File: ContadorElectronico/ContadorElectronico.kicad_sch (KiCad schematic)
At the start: 25 parts, among them J1 Screw_Terminal_01x02, J2 Screw_Terminal_01x02, SW1 MODE, SW2 INC, SW3 DEC, U2 L7805, U4 LM358, U5 4N35, U6 4N35

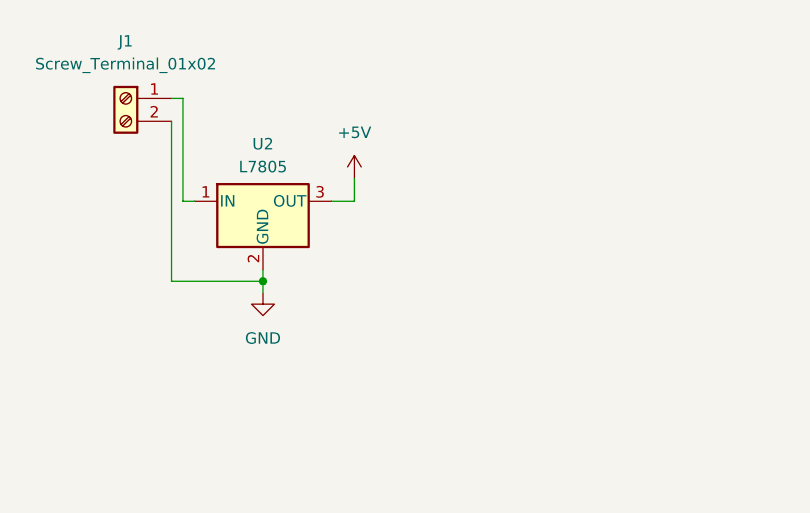
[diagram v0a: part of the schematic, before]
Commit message: Creación simbolo regulador 2596
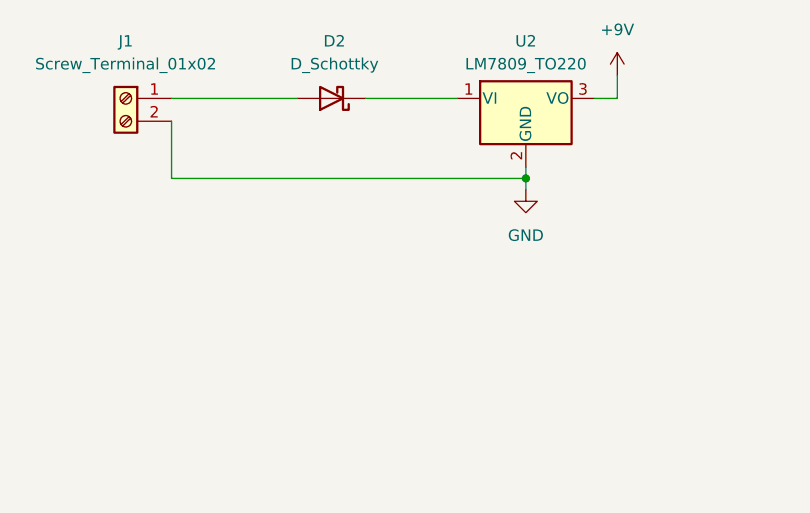
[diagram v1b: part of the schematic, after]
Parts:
- removed U2: L7805, Package_TO_SOT_THT:TO-220-3_Vertical, symbol Regulator_Linear:L7805
- added D2: D_Schottky, Diode_THT:D_DO-15_P12.70mm_Horizontal, symbol Device:D_Schottky
- added U2: LM7809_TO220, Package_TO_SOT_THT:TO-220-3_Vertical, symbol Regulator_Linear:LM7809_TO220
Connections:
- net GND: now also U2.2 (GND)
- net at J1.1 (Pin_1): now also D2.2 (A)
- new net: D2.1 (K), U2.1 (VI)
- new net +9V: U2.3 (VO)

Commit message: xd
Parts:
- removed U2: LM7809_TO220, Package_TO_SOT_THT:TO-220-3_Vertical, symbol Regulator_Linear:LM7809_TO220
- added F?: Fuse, symbol Device:Fuse
- added U?: ~, symbol Custom:LM2596_MODULE
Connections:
- net +5V: now also U?.4 (OUT+)
- net GND: now also U?.3 (OUT-); no longer J1.2 (Pin_2)
- net at D2.1 (K): now also U?.1 (IN+)
- new net: F?.2, U?.2 (IN-)
- new net: F?.1, J1.2 (Pin_2)
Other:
- moved on the sheet: D2, J1
